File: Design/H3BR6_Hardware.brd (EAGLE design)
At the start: 60 x 34.6 mm, 64 parts, among them P2 HEXABIT_X2_P1_P5, Q10 MMBT3904LT1, Q11 MMBT3904LT1, Q12 MMBT3904LT1, Q13 MMBT3904LT1, Q14 MMBT3904LT1, Q7 MMBT3904LT1, Q8 MMBT3904LT1, Q9 MMBT3904LT1, U1 STM32F072CBT6STMICROELECTRONI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, X1 XTALL_CSTCE8M00G52

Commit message: Release REV0
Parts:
- U1: value STM32F072CBT6STMICROELECTRONICS_STM32F072CBT6_0_0 -> (none); device HEXABITZ_ICs:STM32F072CBT6 -> HEXABITZ_ICs:STM32F091CBU6
- moved C7 4.51 mm to (14.6, 18.0), turned to 180 degrees
- moved X1 0.95 mm to (10.8, 26.0)
- moved R10 0.88 mm to (11.0, 15.3), turned to 270 degrees
- moved C6 0.73 mm to (18.3, 16.0)
- moved R18 0.65 mm to (24.0, 12.4)
- moved C4 0.56 mm to (9.76, 12.3)
- moved B 0.48 mm to (4.29, 18.7)
- moved C3 0.40 mm to (8.73, 14.4)
- moved C9 0.32 mm to (5.08, 24.4)
- moved R3 0.32 mm to (3.65, 21.0)
- moved R9 0.32 mm to (13.7, 28.3)
- moved R20 0.32 mm to (37.8, 22.5)
- moved Q15 0.24 mm to (56.6, 20.3)
- moved R14 0.24 mm to (31.8, 16.9)
- moved R15 0.24 mm to (25.1, 16.9)
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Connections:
- net A: now also U1.P$43; no longer U1.43
- net B: now also U1.P$16; no longer U1.16
- net C: now also U1.P$17; no longer U1.17
- net CA1: now also U1.P$38; no longer U1.38
- net CA2: now also U1.P$45; no longer U1.45
- net CA3: now also U1.P$41; no longer U1.41
- net CA4: now also U1.P$42; no longer U1.42
- net CA5: now also U1.P$26; no longer U1.26
- net CA6: now also U1.P$27; no longer U1.27
- net C_LED: now also U1.P$25; no longer U1.25
- net D: now also U1.P$19; no longer U1.19
- net DP: now also U1.P$18; no longer U1.18
- net E: now also U1.P$20; no longer U1.20
- net F: now also U1.P$46; no longer U1.46
- net G: now also U1.P$28; no longer U1.28
- net GND: now also U1.EP, U1.P$23, U1.P$35, U1.P$47; no longer U1.23, U1.35, U1.47
- net N$2: now also U1.P$32; no longer U1.32
- net N$3: now also U1.P$34; no longer U1.34
- net N$4: now also U1.P$37; no longer U1.37
- net N$5: now also U1.P$3; no longer U1.3
- net N$6: now also U1.P$4; no longer U1.4
- net N$7: now also U1.P$44; no longer U1.44
- net N$8: now also U1.P$7; no longer U1.7
- net USART1_RX: now also U1.P$31; no longer U1.31
- net USART1_TX: now also U1.P$30; no longer U1.30
- net USART2_RX: now also U1.P$13; no longer U1.13
- net USART2_TX: now also U1.P$12; no longer U1.12
- net USART3_RX: now also U1.P$22; no longer U1.22
- net USART3_TX: now also U1.P$21; no longer U1.21
- net USART4_RX: now also U1.P$11; no longer U1.11
- net USART4_TX: now also U1.P$10; no longer U1.10
- net USART5_RX: now also U1.P$40; no longer U1.40
- net USART5_TX: now also U1.P$39; no longer U1.39
- net USART6_RX: now also U1.P$15; no longer U1.15
- net USART6_TX: now also U1.P$14; no longer U1.14
- net VDD: now also U1.P$1, U1.P$24, U1.P$36, U1.P$48; no longer U1.1, U1.24, U1.36, U1.48
- net VDDA: now also U1.P$9; no longer U1.9
- net VSSA: now also U1.P$8; no longer U1.8
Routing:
- net CA3: track 24.3 -> 35.7 mm
- net GND: track 116.6 -> 107.9 mm, vias 7 -> 6
- net VDD: track 82.1 -> 73.6 mm, vias 8 -> 7
- net USART3_TX: track 21.6 -> 24.5 mm
- net N$4: track 5.62 -> 7.59 mm
- net USART1_TX: track 15.9 -> 17.8 mm
- net N$7: track 8.65 -> 9.97 mm
- net USART3_RX: track 17.1 -> 18.3 mm
- net CA2: track 20.2 -> 21.3 mm
- net G: track 10.00 -> 8.98 mm
- net N$8: track 13.0 -> 13.9 mm
- net N$44: track 30.1 -> 29.1 mm
- net F: track 14.8 -> 15.8 mm
- net A: track 7.06 -> 7.99 mm
- net USART6_TX: track 15.0 -> 15.9 mm
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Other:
- board text added: "H3BR60"

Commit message: FIX Rev0
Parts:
- moved R13 0.08 mm to (35.8, 24.0)
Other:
- board text added: "B"
- board text added: "C"
- board text added: "D"
- board text added: "R"

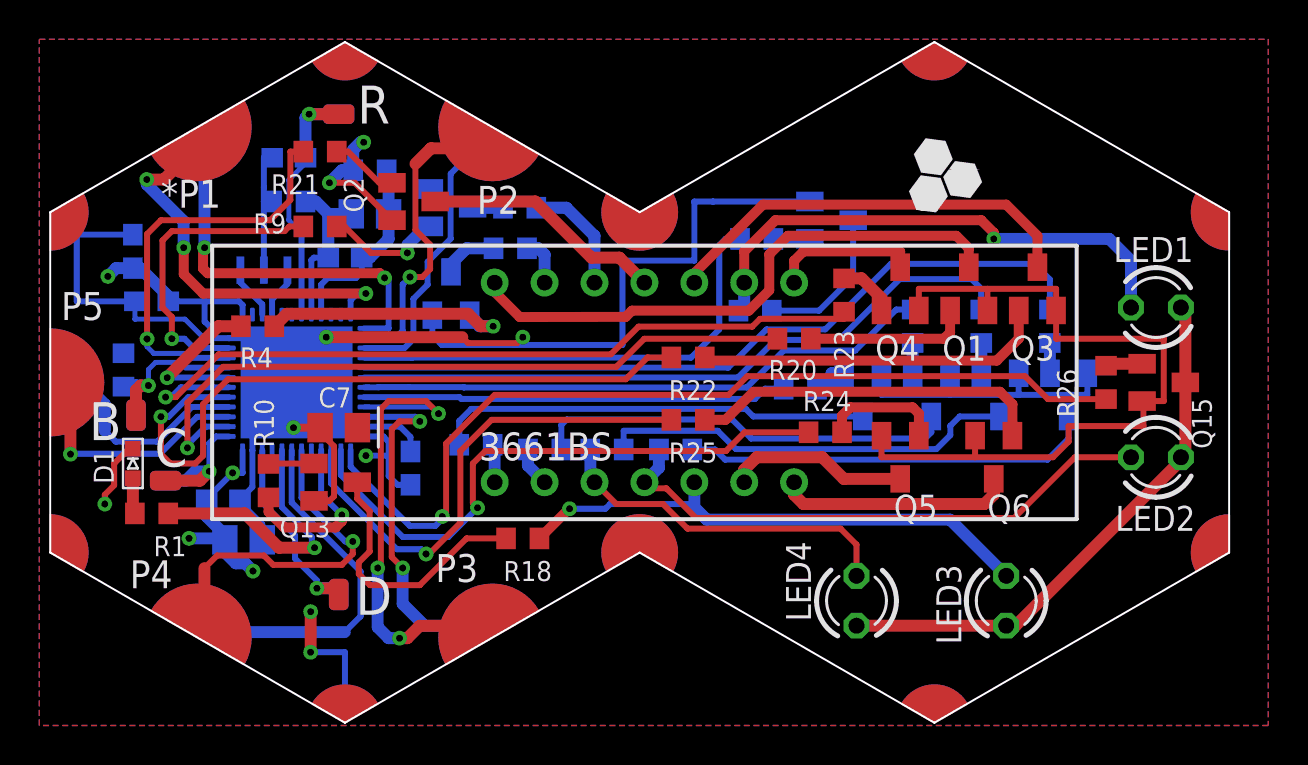
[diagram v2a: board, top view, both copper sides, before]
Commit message: -Changing the MC with STM32G0
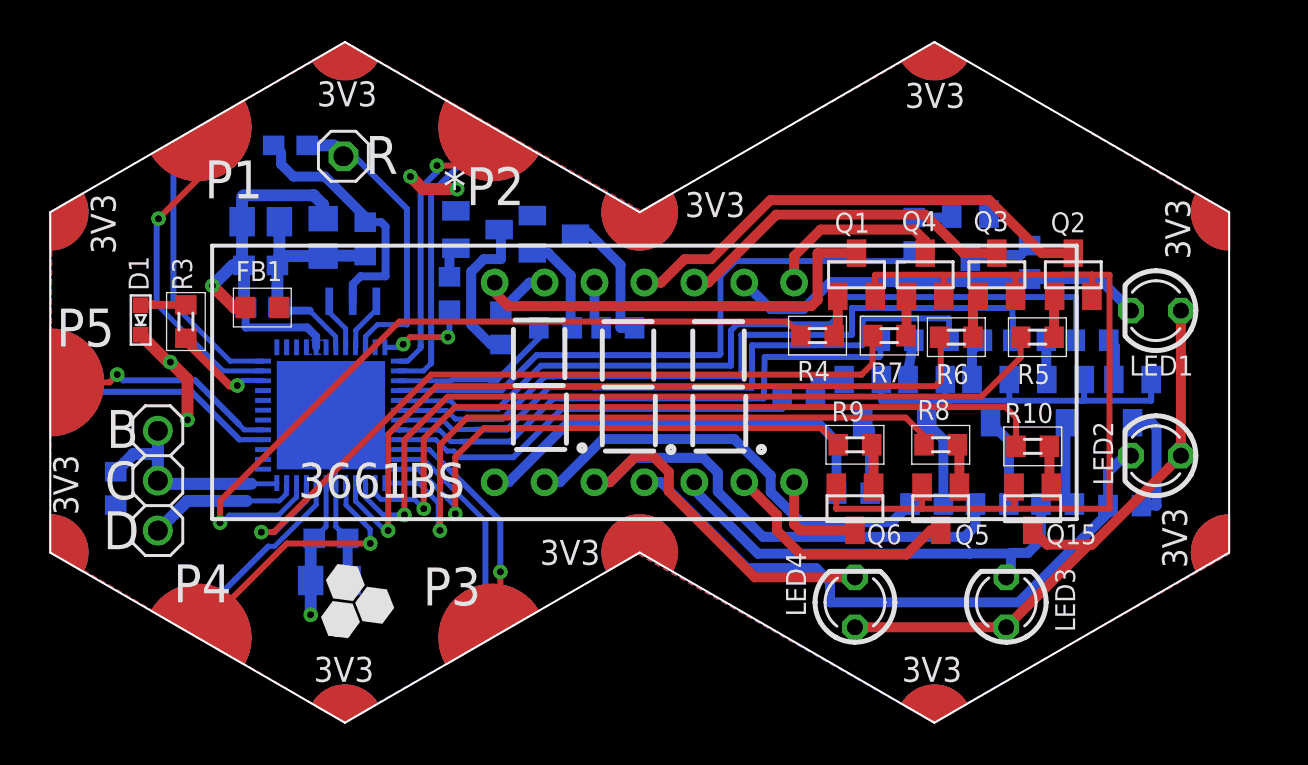
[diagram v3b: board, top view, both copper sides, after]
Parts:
- removed B, C, D, R: PAD1, Hexabitz:PAD1
- removed C8, C9: 100nF, Hexabitz:C-0603
- added JP1: R, HEXABITZ_USER_INTERFACE_PARTS:1X01
- added JP2: (no value), pinhead:1X03
- C1: value 10nF -> 100nF; device Hexabitz:C-0603 -> HEXABITZ_RCLS:C-0603
- C2: value 1.00uF -> 4.7uF; device Hexabitz:C-0805-POL -> HEXABITZ_RCLS:C-0805-POL
- C3, C5, C6: device Hexabitz:C-0603 -> HEXABITZ_RCLS:C-0603
- C4: value 4.7uF -> 1uF; device Hexabitz:C-0805-POL -> HEXABITZ_RCLS:C-0805-POL
- C7: device Hexabitz:C-0805-POL -> HEXABITZ_RCLS:C-0805-POL
- FB1: value FB-TDK_MMZ1608Y300B -> (none); device Hexabitz:FB-TDK_MMZ1608Y300B -> HEXABITZ_RCLS:FB-0603
- LED1, LED2, LED3, LED4: device HEXABITZ_RCLS:LED3MM -> led:LED3MM
- R1: value 270.0R -> 10K; device Hexabitz:R-0603 -> HEXABITZ_RCLS:R-0603
- R10, R11, R20, R21, R22, R23, R24, R25, R26, R4, R5, R6, R7, R8, R9: value 10K -> 10k; device Hexabitz:R-0603 -> HEXABITZ_RCLS:R-0603
- R12, R13, R14, R15, R16, R17, R18, R19, R2: device Hexabitz:R-0603 -> HEXABITZ_RCLS:R-0603
- R3: value 10.0K -> 270R; device Hexabitz:R-0603 -> HEXABITZ_RCLS:R-0603
- U1: value (none) -> STM32G0B1CEU6NUFQFPN48_STM32_STM; device HEXABITZ_ICs:STM32F091CBU6 -> HEXABITZ_ICs:UFQFPN48_STM32_STM
- moved R10 38.9 mm to (49.9, 17.1), turned to 0 degrees
- moved Q13 37.4 mm to (51.6, 19.4), flipped to the bottom, turned to 180 degrees
- moved Q2 33.8 mm to (52.0, 25.8), turned to 0 degrees
- moved R26 33.7 mm to (20.2, 24.8), flipped to the bottom, turned to 90 degrees
- moved R9 29.4 mm to (40.9, 17.1), turned to 0 degrees
- moved R4 28.5 mm to (39.0, 22.7), turned to 0 degrees
- moved R18 27.3 mm to (51.2, 14.1), flipped to the bottom, turned to 0 degrees
- moved R14 23.0 mm to (54.6, 14.0), turned to 0 degrees
- moved R19 19.8 mm to (47.9, 14.1), turned to 0 degrees
- moved R15 19.6 mm to (44.5, 14.1), turned to 0 degrees
- moved R16 19.4 mm to (40.8, 14.7)
- moved C5 17.7 mm to (14.2, 12.4), turned to 180 degrees
- moved C6 17.5 mm to (12.1, 32.4), turned to 0 degrees
- moved C4 16.2 mm to (10.6, 28.5)
- moved R5 15.1 mm to (50.2, 22.6), flipped to the top
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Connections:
- removed net N$3: D.P$1, D.P$2, U1.P$34
- removed net N$4: C.P$1, C.P$2, U1.P$37
- removed net N$7: B.P$1, B.P$2, R3.2, U1.P$44
- removed net USART4_RX: U1.P$11
- removed net USART4_TX: U1.P$10
- new net CLK: JP2.1, JP2.2, R1.2, U1.36
- new net DATA: JP2.3, U1.35
- net A: now also R26.1, U1.12; no longer R4.2, U1.P$43
- net B: now also R25.1, U1.16; no longer R5.2, U1.P$16
- net C: now also R24.1, U1.17; no longer R6.2, U1.P$17
- net CA1: now also R4.1, U1.34; no longer R20.2, U1.P$38
- net CA2: now also R5.1, U1.27; no longer R21.2, U1.P$45
- net CA3: now also R6.1, U1.28; no longer R22.2, U1.P$41
- net CA4: now also R7.1, U1.33; no longer R23.2, U1.P$42
- net CA5: now also R8.1, U1.25; no longer R24.2, U1.P$26
- net CA6: now also R9.1, U1.24; no longer R25.2, U1.P$27
- net C_LED: now also R10.1, U1.26; no longer R26.2, U1.P$25
- net D: now also R23.1, U1.20; no longer R7.2, U1.P$19
- net DP: now also R11.1, U1.19; no longer R11.2, U1.P$18
- net E: now also R22.1, U1.21; no longer R8.2, U1.P$20
- net F: now also R21.1, U1.15; no longer R9.2, U1.P$46
- net G: now also R20.1, U1.18; no longer R10.2, U1.P$28
- net GND: now also R1.1, R2.2, U1.1, U1.2, U1.30, U1.37, U1.38, U1.49; no longer C3.2, C4.2, C8.2, C9.2, R2.1, R3.1, U1.EP, U1.P$23, U1.P$35, U1.P$47
- net N$1: now also R3.2; no longer R1.1
- net N$10: now also R25.2; no longer R5.1
- net N$11: now also R24.2; no longer R6.1
- net N$12: now also R23.2; no longer R7.1
- net N$13: now also R22.2; no longer R8.1
- net N$14: now also R21.2; no longer R9.1
- net N$15: now also R20.2; no longer R10.1
- net N$16: now also R11.2; no longer R11.1
- net N$17: now also R12.1; no longer R12.2
- net N$18: now also R13.1; no longer R13.2
- net N$19: now also R14.1; no longer R14.2
- net N$2: now also R3.1, U1.46; no longer R1.2, U1.P$32
- net N$20: now also R15.1; no longer R15.2
- net N$21: now also R16.1; no longer R16.2
- net N$22: now also R17.1; no longer R17.2
- net N$23: now also R18.1; no longer R18.2
- net N$24: now also R19.1; no longer R19.2
- net N$25: now also R4.2; no longer R20.1
- net N$26: now also R5.2; no longer R21.1
- net N$27: now also R6.2; no longer R22.1
- net N$28: now also R7.2; no longer R23.1
- net N$29: now also R8.2; no longer R24.1
- net N$30: now also R9.2; no longer R25.1
- net N$31: now also R19.2; no longer R19.1
- net N$32: now also R18.2; no longer R18.1
- net N$33: now also R17.2; no longer R17.1
- net N$34: now also R16.2; no longer R16.1
- net N$35: now also R15.2; no longer R15.1
- net N$36: now also R14.2; no longer R14.1
- net N$37: now also R13.2; no longer R13.1
- net N$38: now also R12.2; no longer R12.1
- net N$45: now also R10.2; no longer R26.1
- net N$5: now also U1.9; no longer U1.P$3
- net N$6: now also U1.8; no longer U1.P$4
- net N$8: now also C6.1, JP1.1, U1.10; no longer C8.1, R.P$1, R.P$2, U1.P$7
- net N$9: now also R26.2; no longer R4.1
- net USART1_RX: now also U1.32; no longer U1.P$31
- net USART1_TX: now also U1.29; no longer U1.P$30
- net USART2_RX: now also P2.PAD_PD2, U1.14; no longer P2.PAD_PD1, U1.P$13
- net USART2_TX: now also P2.PAD_PU2, U1.13; no longer P2.PAD_PU1, U1.P$12
- net USART3_RX: now also U1.23; no longer U1.P$22
- net USART3_TX: now also U1.22; no longer U1.P$21
- net USART5_RX: now also U1.40; no longer U1.P$40
- net USART5_TX: now also U1.41; no longer U1.P$39
- net USART6_RX: now also P2.PAD_PD1, U1.48; no longer P2.PAD_PD2, U1.P$15
- net USART6_TX: now also P2.PAD_PU1, U1.47; no longer P2.PAD_PU2, U1.P$14
- net VDD: now also U1.31; no longer C3.1, C4.1, C6.1, C9.1, U1.P$1, U1.P$24, U1.P$36, U1.P$48
- net VDDA: now also C3.1, C4.1, U1.4, U1.5, U1.6; no longer U1.P$9
- net VSSA: now also C3.2, C4.2, R2.1, U1.7; no longer R2.2, U1.P$8
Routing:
- net GND: track 107.9 -> 49.3 mm, vias 6 -> 4
- net G: track 8.98 -> 37.5 mm, vias 1 -> 0
- net N$31: track 18.0 -> 40.4 mm
- net VDD: track 73.4 -> 52.7 mm, vias 7 -> 1
- net N$35: track 2.02 -> 22.1 mm
- net CA2: track 21.3 -> 41.0 mm
- net N$34: track 1.95 -> 21.6 mm
- net N$21: track 22.2 -> 3.74 mm
- net N$20: track 21.5 -> 4.49 mm
- net N$24: track 21.5 -> 4.52 mm
- net N$30: track 18.1 -> 2.20 mm
- net N$27: track 17.9 -> 2.34 mm
- net N$19: track 20.9 -> 6.06 mm
- net N$43: track 12.4 -> 24.7 mm
- net USART3_TX: track 24.5 -> 12.3 mm, vias 3 -> 1
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- added copper zone on layer 16, net VDDA
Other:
- board text added: "*"
- board text added: "*P2"
- board text added: "3661BS"
- board text added: "3V3"
- board text added: "GND"
- board text added: "H3BR61"
- board text added: "P1"
- board text removed: "*P1"
- board text removed: "H3BR60"
- board text removed: "P2"
